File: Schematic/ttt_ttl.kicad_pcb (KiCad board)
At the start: 2 copper layers, 81.8 x 146.8 mm, 86 parts, among them SW1 SW_Push, SW10 SW_Push, SW2 SW_Push, SW3 SW_Push, SW4 SW_Push, SW5 SW_Push, SW6 SW_Push, SW7 SW_Push, SW8 SW_Push, SW9 SW_Push, U1 74LS107, U10 27C020, U11 74LS154, U12 NE555, U2 74LS107, U3 74LS107, U4 74LS107, U5 74LS107, U6 74LS107, U7 74LS107, U8 74LS107, U9 74LS107

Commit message: More work on the circuit and the PCB layout.
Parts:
- removed R13, R15, R20, R22, R24: 10K, Resistor_THT:R_Axial_DIN0204_L3.6mm_D1.6mm_P1.90mm_Vertical
- removed R14, R19, R21, R23: 1K, Resistor_THT:R_Axial_DIN0204_L3.6mm_D1.6mm_P1.90mm_Vertical
- R11, R2, R28, R29, R30, R31, R32, R33, R34, R35, R36, R4, R6: value 10K -> 1K
- U1, U2, U3, U4, U5, U6, U7, U8, U9: value 74LS107 -> 74LS109
- moved R5 66.5 mm to (65.0, 46.5), turned to 0 degrees
- moved R2 58.7 mm to (39.1, 106.2), turned to 0 degrees
- moved R11 41.7 mm to (93.7, 76.7), turned to 0 degrees
- moved R12 35.2 mm to (93.5, 105.4), turned to 0 degrees
- moved SW5 32.0 mm to (61.0, 50.0)
- moved SW4 28.5 mm to (61.0, 79.2)
- moved R4 27.1 mm to (65.5, 75.9), turned to 0 degrees
- moved R6 26.9 mm to (66.3, 105.7), turned to 0 degrees
- moved R10 25.0 mm to (93.2, 46.7), turned to 0 degrees
- moved C1 20.9 mm to (88.5, 144.3)
- moved U12 20.9 mm to (76.8, 136.7)
- moved C2 20.9 mm to (98.9, 136.5)
- moved R41 20.9 mm to (90.9, 136.5)
- moved R42 20.9 mm to (72.4, 141.5)
- moved R40 18.5 mm to (42.5, 144.0)
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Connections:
- R1 pad 1: Hi -> Net-(R1-Pad1)
- R1 pad 2: Net-(R1-Pad2) -> Lo
- R10 pad 1: Hi -> Net-(R10-Pad1)
- R10 pad 2: Net-(R10-Pad2) -> Lo
- R11 pad 1: Net-(R10-Pad2) -> Net-(R11-Pad1)
- R12 pad 1: Hi -> Net-(R12-Pad1)
- R12 pad 2: Net-(R12-Pad2) -> Lo
- R2 pad 1: Net-(R1-Pad2) -> Net-(R2-Pad1)
- R3 pad 1: Hi -> Net-(R3-Pad1)
- R3 pad 2: Net-(R3-Pad2) -> Lo
- R4 pad 1: Net-(R3-Pad2) -> Net-(R4-Pad1)
- R5 pad 1: Hi -> Net-(R5-Pad1)
- R5 pad 2: Net-(R5-Pad2) -> Lo
- R6 pad 1: Net-(R5-Pad2) -> Net-(R6-Pad1)
- SW1 pad 1: Net-(R1-Pad2) -> Hi
- SW1 pad 2: Net-(SW1-Pad2) -> Net-(R1-Pad1)
- SW2 pad 1: Net-(R3-Pad2) -> Hi
- SW2 pad 2: Net-(SW2-Pad2) -> Net-(R3-Pad1)
- SW3 pad 1: Net-(R5-Pad2) -> Hi
- SW3 pad 2: Net-(SW3-Pad2) -> Net-(R2-Pad1)
- SW4 pad 1: Net-(R10-Pad2) -> Hi
- SW4 pad 2: Net-(SW4-Pad2) -> Net-(R4-Pad1)
- SW5 pad 1: Net-(R12-Pad2) -> Hi
- SW5 pad 2: Net-(SW5-Pad2) -> Net-(R5-Pad1)
- SW6 pad 1: Net-(R14-Pad2) -> Hi
- SW6 pad 2: Net-(SW6-Pad2) -> Net-(R6-Pad1)
- SW7 pad 1: Net-(R19-Pad2) -> Hi
- SW7 pad 2: Net-(SW7-Pad2) -> Net-(R10-Pad1)
- SW8 pad 1: Net-(R21-Pad2) -> Hi
- SW8 pad 2: Net-(SW8-Pad2) -> Net-(R11-Pad1)
- SW9 pad 1: Net-(R23-Pad2) -> Hi
- SW9 pad 2: Net-(SW9-Pad2) -> Net-(R12-Pad1)
- U1 pad 1: Net-(SW1-Pad2) -> Net-(R1-Pad1)
- U1 pad 11: Net-(U1-Pad11) -> Move1
- U1 pad 5: Board1 -> Net-(U1-Pad5)
- U1 pad 6: Net-(U1-Pad6) -> Board1
- U1 pad 8: Move1 -> Lo
- U2 pad 1: Net-(SW4-Pad2) -> Net-(R5-Pad1)
- U2 pad 11: Net-(U2-Pad11) -> Move2
- U2 pad 5: Board2 -> Net-(U2-Pad5)
- U2 pad 6: Net-(U2-Pad6) -> Board2
- U2 pad 8: Move2 -> Lo
- U3 pad 1: Net-(SW7-Pad2) -> Net-(R10-Pad1)
- U3 pad 11: Net-(U3-Pad11) -> Move3
- U3 pad 5: Board3 -> Net-(U3-Pad5)
- U3 pad 6: Net-(U3-Pad6) -> Board3
- U3 pad 8: Move3 -> Lo
- U4 pad 1: Net-(SW2-Pad2) -> Net-(R3-Pad1)
- U4 pad 11: Net-(U4-Pad11) -> Move4
- U4 pad 5: Board4 -> Net-(U4-Pad5)
- U4 pad 6: Net-(U4-Pad6) -> Board4
- U4 pad 8: Move4 -> Lo
- U5 pad 1: Net-(SW5-Pad2) -> Net-(R4-Pad1)
- U5 pad 11: Net-(U5-Pad11) -> Move5
- U5 pad 5: Board5 -> Net-(U5-Pad5)
- U5 pad 6: Net-(U5-Pad6) -> Board5
- U5 pad 8: Move5 -> Lo
- U6 pad 1: Net-(SW8-Pad2) -> Net-(R11-Pad1)
- U6 pad 11: Net-(U6-Pad11) -> Move6
- U6 pad 5: Board6 -> Net-(U6-Pad5)
- U6 pad 6: Net-(U6-Pad6) -> Board6
- U6 pad 8: Move6 -> Lo
- U7 pad 1: Net-(SW3-Pad2) -> Net-(R2-Pad1)
- U7 pad 11: Net-(U7-Pad11) -> Move7
- U7 pad 5: Board7 -> Net-(U7-Pad5)
- U7 pad 6: Net-(U7-Pad6) -> Board7
- U7 pad 8: Move7 -> Lo
- U8 pad 1: Net-(SW6-Pad2) -> Net-(R6-Pad1)
- U8 pad 11: Net-(U8-Pad11) -> Move8
- U8 pad 5: Board8 -> Net-(U8-Pad5)
- U8 pad 6: Net-(U8-Pad6) -> Board8
- U8 pad 8: Move8 -> Lo
- U9 pad 1: Net-(SW9-Pad2) -> Net-(R12-Pad1)
- U9 pad 11: Net-(U9-Pad11) -> Move9
- U9 pad 5: Board9 -> Net-(U9-Pad5)
- U9 pad 6: Net-(U9-Pad6) -> Board9
- U9 pad 8: Move9 -> Lo
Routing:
- net Lo: track 462.8 -> 0.00 mm
- net Hi: track 446.4 -> 0.00 mm
- net Reset: track 342.6 -> 0.00 mm
- net Clk: track 329.7 -> 0.00 mm
- net User1: track 157.1 -> 0.00 mm
- net User3: track 135.0 -> 0.00 mm
- net Board3: track 128.9 -> 0.00 mm
- net User2: track 121.2 -> 0.00 mm
- net Move1: track 117.1 -> 0.00 mm, vias 1 -> 0
- net Board6: track 116.4 -> 0.00 mm, vias 1 -> 0
- net User6: track 111.1 -> 0.00 mm, vias 1 -> 0
- net Board2: track 107.6 -> 0.00 mm
- net Board1: track 106.2 -> 0.00 mm
- net Move2: track 100.6 -> 0.00 mm
- net Move4: track 100.5 -> 0.00 mm, vias 1 -> 0
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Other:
- net class Power added: clearance 0.4064, trace_width 0.508, via_dia 1.524, via_drill 0.762

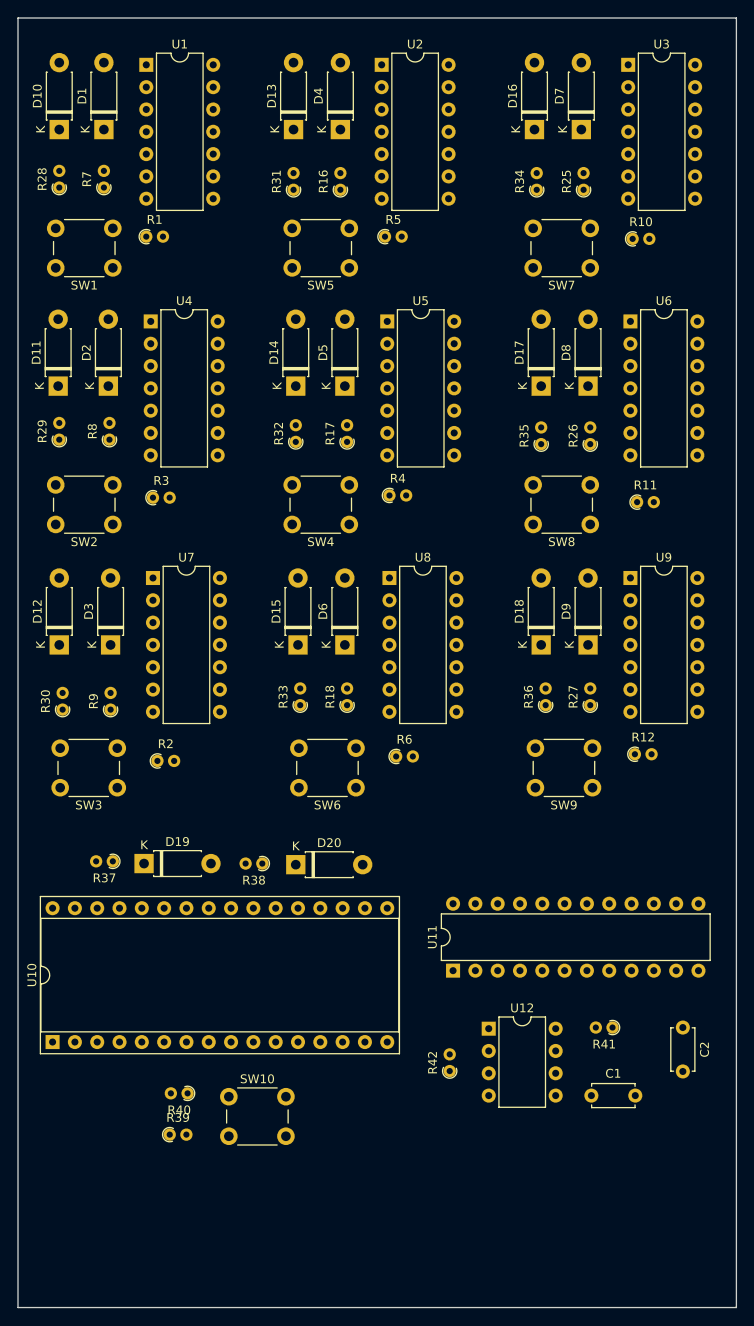
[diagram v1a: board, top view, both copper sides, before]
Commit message: Fixed up the reset line circuitry
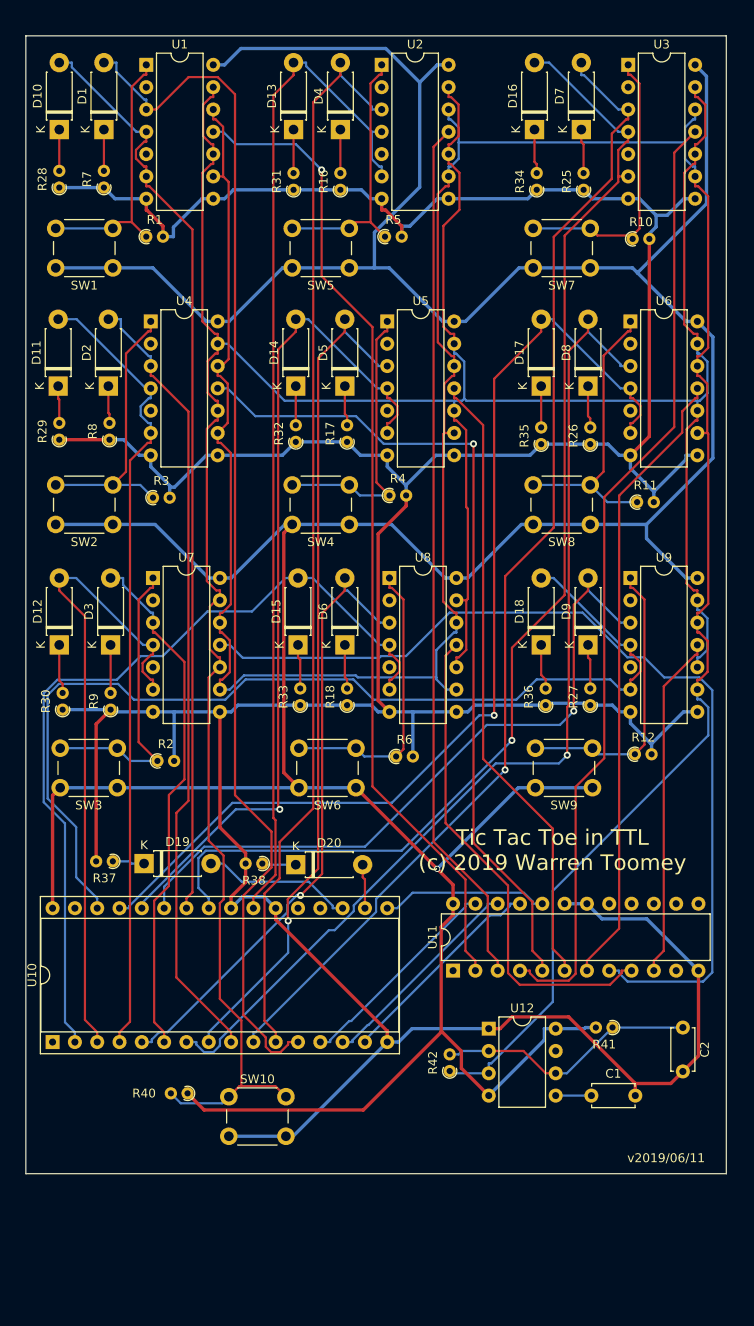
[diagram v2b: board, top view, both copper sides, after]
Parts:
- removed R39: 10K, Resistor_THT:R_Axial_DIN0204_L3.6mm_D1.6mm_P1.90mm_Vertical
- R16, R17, R18, R25, R26, R27, R7, R8, R9: value 10K -> 1K
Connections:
- R40 pad 1: Net-(R39-Pad2) -> Hi
- R40 pad 2: Lo -> Reset
- SW10 pad 1: Net-(R39-Pad2) -> Reset
- SW10 pad 2: Reset -> Lo
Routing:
- net Lo: track 0.00 -> 485.2 mm
- net Hi: track 0.00 -> 472.3 mm, vias 0 -> 1
- net Reset: track 0.00 -> 340.9 mm
- net Clk: track 0.00 -> 330.2 mm
- net User1: track 0.00 -> 137.9 mm
- net Board3: track 0.00 -> 137.4 mm, vias 0 -> 1
- net User3: track 0.00 -> 132.5 mm, vias 0 -> 1
- net User2: track 0.00 -> 123.6 mm
- net Board6: track 0.00 -> 119.1 mm, vias 0 -> 1
- net Board2: track 0.00 -> 117.6 mm
- net User6: track 0.00 -> 117.4 mm, vias 0 -> 1
- net Board9: track 0.00 -> 117.2 mm
- net Move1: track 0.00 -> 112.6 mm, vias 0 -> 1
- net Move3: track 0.00 -> 108.8 mm
- net Move7: track 0.00 -> 107.4 mm
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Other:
- board size 81.8 x 146.8 mm -> 79.8 x 129.5 mm
- net class Power: clearance 0.4064 -> 0.299979; trace_width 0.508 -> 0.381; via_dia 1.524 -> 0.7; via_drill 0.762 -> 0.5
- board text added: "Tic Tac Toe in TTL (c) 2019 Warren Toomey"
- board text added: "v2019/06/11"

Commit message: Updated the schematic and PCB with the new flip-flip pinouts and footprints.
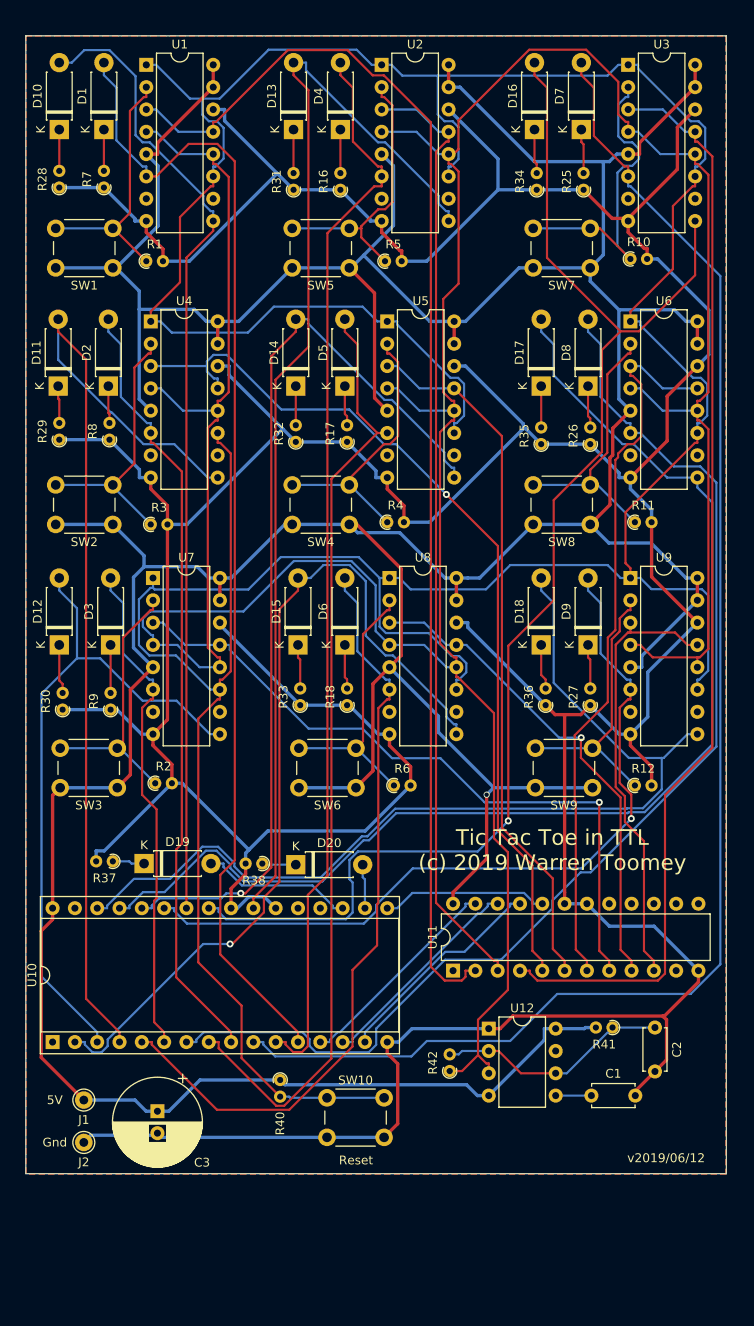
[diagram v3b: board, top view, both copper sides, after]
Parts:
- added C3: 220uF, Capacitor_THT:CP_Radial_D10.0mm_P2.50mm, F.Cu at (39.1, 146.1)
- added J1: Conn_01x01, Connector_Pin:Pin_D1.0mm_L10.0mm, F.Cu at (30.7, 144.8)
- added J2: Conn_01x01, Connector_Pin:Pin_D1.0mm_L10.0mm, F.Cu at (30.7, 149.6)
- U1, U2, U3, U4, U5, U6, U7, U8, U9: footprint Package_DIP:DIP-14_W7.62mm -> Package_DIP:DIP-16_W7.62mm
- moved SW10 11.2 mm to (58.4, 144.5)
- moved R40 10.7 mm to (53.1, 142.5), turned to 270 degrees
- moved R12 3.56 mm to (93.5, 109.0)
- moved R6 3.31 mm to (66.0, 109.0)
- moved C2 3.18 mm to (95.8, 136.5)
- moved R3 3.06 mm to (38.4, 79.2)
- moved R4 3.06 mm to (65.3, 79.0)
- moved R1 2.79 mm to (37.8, 49.3)
- moved R5 2.79 mm to (65.0, 49.3)
- moved R2 2.55 mm to (38.9, 108.7)
- moved R10 2.30 mm to (93.0, 49.0)
- moved R11 2.30 mm to (93.5, 79.0)
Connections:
- U1 pad 1: Net-(R1-Pad1) -> Reset
- U1 pad 10: Reset -> Net-(U1-Pad10)
- U1 pad 11: Move1 -> Reset
- U1 pad 13: Reset -> Move1
- U1 pad 14: Hi -> Lo
- U1 pad 2: Net-(U1-Pad2) -> Net-(R1-Pad1)
- U1 pad 3: User1 -> Move1
- U1 pad 4: Board1 -> Clk
- U1 pad 5: Net-(U1-Pad5) -> Hi
- U1 pad 6: Board1 -> User1
- U1 pad 7: Lo -> Net-(U1-Pad7)
- U1 pad 9: Clk -> Board1
- U2 pad 1: Net-(R5-Pad1) -> Reset
- U2 pad 10: Reset -> Net-(U2-Pad10)
- U2 pad 11: Move2 -> Reset
- U2 pad 13: Reset -> Move2
- U2 pad 14: Hi -> Lo
- U2 pad 2: Net-(U2-Pad2) -> Net-(R5-Pad1)
- U2 pad 3: User2 -> Move2
- U2 pad 4: Board2 -> Clk
- U2 pad 5: Net-(U2-Pad5) -> Hi
- U2 pad 6: Board2 -> User2
- U2 pad 7: Lo -> Net-(U2-Pad7)
- U2 pad 9: Clk -> Board2
- U3 pad 1: Net-(R10-Pad1) -> Reset
- U3 pad 10: Reset -> Net-(U3-Pad10)
- U3 pad 11: Move3 -> Reset
- U3 pad 13: Reset -> Move3
- U3 pad 14: Hi -> Lo
- U3 pad 2: Net-(U3-Pad2) -> Net-(R10-Pad1)
- U3 pad 3: User3 -> Move3
- U3 pad 4: Board3 -> Clk
- U3 pad 5: Net-(U3-Pad5) -> Hi
- U3 pad 6: Board3 -> User3
- U3 pad 7: Lo -> Net-(U3-Pad7)
- U3 pad 9: Clk -> Board3
- U4 pad 1: Net-(R3-Pad1) -> Reset
- U4 pad 10: Reset -> Net-(U4-Pad10)
- U4 pad 11: Move4 -> Reset
- U4 pad 13: Reset -> Move4
- U4 pad 14: Hi -> Lo
- U4 pad 2: Net-(U4-Pad2) -> Net-(R3-Pad1)
- U4 pad 3: User4 -> Move4
- U4 pad 4: Board4 -> Clk
- U4 pad 5: Net-(U4-Pad5) -> Hi
- U4 pad 6: Board4 -> User4
- U4 pad 7: Lo -> Net-(U4-Pad7)
- U4 pad 9: Clk -> Board4
- U5 pad 1: Net-(R4-Pad1) -> Reset
- U5 pad 10: Reset -> Net-(U5-Pad10)
- U5 pad 11: Move5 -> Reset
- U5 pad 13: Reset -> Move5
- U5 pad 14: Hi -> Lo
- U5 pad 2: Net-(U5-Pad2) -> Net-(R4-Pad1)
- U5 pad 3: User5 -> Move5
- U5 pad 4: Board5 -> Clk
- U5 pad 5: Net-(U5-Pad5) -> Hi
- U5 pad 6: Board5 -> User5
- U5 pad 7: Lo -> Net-(U5-Pad7)
- U5 pad 9: Clk -> Board5
- U6 pad 1: Net-(R11-Pad1) -> Reset
- U6 pad 10: Reset -> Net-(U6-Pad10)
- U6 pad 11: Move6 -> Reset
- U6 pad 13: Reset -> Move6
- U6 pad 14: Hi -> Lo
- U6 pad 2: Net-(U6-Pad2) -> Net-(R11-Pad1)
- U6 pad 3: User6 -> Move6
- U6 pad 4: Board6 -> Clk
- U6 pad 5: Net-(U6-Pad5) -> Hi
- U6 pad 6: Board6 -> User6
- U6 pad 7: Lo -> Net-(U6-Pad7)
- U6 pad 9: Clk -> Board6
- U7 pad 1: Net-(R2-Pad1) -> Reset
- U7 pad 10: Reset -> Net-(U7-Pad10)
- U7 pad 11: Move7 -> Reset
- U7 pad 13: Reset -> Move7
- U7 pad 14: Hi -> Lo
- U7 pad 2: Net-(U7-Pad2) -> Net-(R2-Pad1)
- U7 pad 3: User7 -> Move7
- U7 pad 4: Board7 -> Clk
- U7 pad 5: Net-(U7-Pad5) -> Hi
- U7 pad 6: Board7 -> User7
- U7 pad 7: Lo -> Net-(U7-Pad7)
- U7 pad 9: Clk -> Board7
- U8 pad 1: Net-(R6-Pad1) -> Reset
- U8 pad 10: Reset -> Net-(U8-Pad10)
- U8 pad 11: Move8 -> Reset
- U8 pad 13: Reset -> Move8
- U8 pad 14: Hi -> Lo
- U8 pad 2: Net-(U8-Pad2) -> Net-(R6-Pad1)
- U8 pad 3: User8 -> Move8
- U8 pad 4: Board8 -> Clk
- U8 pad 5: Net-(U8-Pad5) -> Hi
- U8 pad 6: Board8 -> User8
- U8 pad 7: Lo -> Net-(U8-Pad7)
- U8 pad 9: Clk -> Board8
- U9 pad 1: Net-(R12-Pad1) -> Reset
- U9 pad 10: Reset -> Net-(U9-Pad10)
- U9 pad 11: Move9 -> Reset
- U9 pad 13: Reset -> Move9
- U9 pad 14: Hi -> Lo
- U9 pad 2: Net-(U9-Pad2) -> Net-(R12-Pad1)
- U9 pad 3: User9 -> Move9
- U9 pad 4: Board9 -> Clk
- U9 pad 5: Net-(U9-Pad5) -> Hi
- U9 pad 6: Board9 -> User9
- U9 pad 7: Lo -> Net-(U9-Pad7)
- U9 pad 9: Clk -> Board9
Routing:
- net Lo: track 485.2 -> 612.1 mm
- net Hi: track 472.3 -> 580.6 mm
- net Reset: track 340.9 -> 443.4 mm
- net Clk: track 330.2 -> 392.9 mm
- net User3: track 132.5 -> 168.0 mm, vias 1 -> 0
- net Move1: track 112.6 -> 144.1 mm, vias 1 -> 0
- net Move7: track 107.4 -> 79.2 mm, vias 0 -> 1
- net Board4: track 91.4 -> 113.5 mm
- net Board3: track 137.4 -> 156.5 mm
- net Board6: track 119.1 -> 137.8 mm, vias 1 -> 0
- net User6: track 117.4 -> 135.8 mm, vias 1 -> 0
- net Move3: track 108.8 -> 125.2 mm
- net User8: track 71.9 -> 87.9 mm, vias 1 -> 0
- net User5: track 96.7 -> 108.6 mm, vias 1 -> 0
- net Move9: track 39.3 -> 50.5 mm
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- added copper zone on B.Cu, net Lo
- added copper zone on F.Cu, net Lo
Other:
- board text added: "5V"
- board text added: "Gnd"
- board text added: "Reset"
- board text added: "v2019/06/12"
- board text removed: "v2019/06/11"

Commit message: Fixed ROM part, was 27C020, should be 27C2001
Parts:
- U10: value 27C020 -> 27C2001
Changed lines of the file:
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@@
       (effects (font (size 1 1) (thickness 0.15)))
     )
-    (fp_text value 27C020 (at 7.62 40.43 90) (layer F.Fab)
+    (fp_text value 27C2001 (at 7.62 40.43 90) (layer F.Fab)
       (effects (font (size 1 1) (thickness 0.15)))
     )
